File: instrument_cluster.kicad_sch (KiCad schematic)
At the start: 8 parts, among them J21 Conn_01x90_3Row_Socket

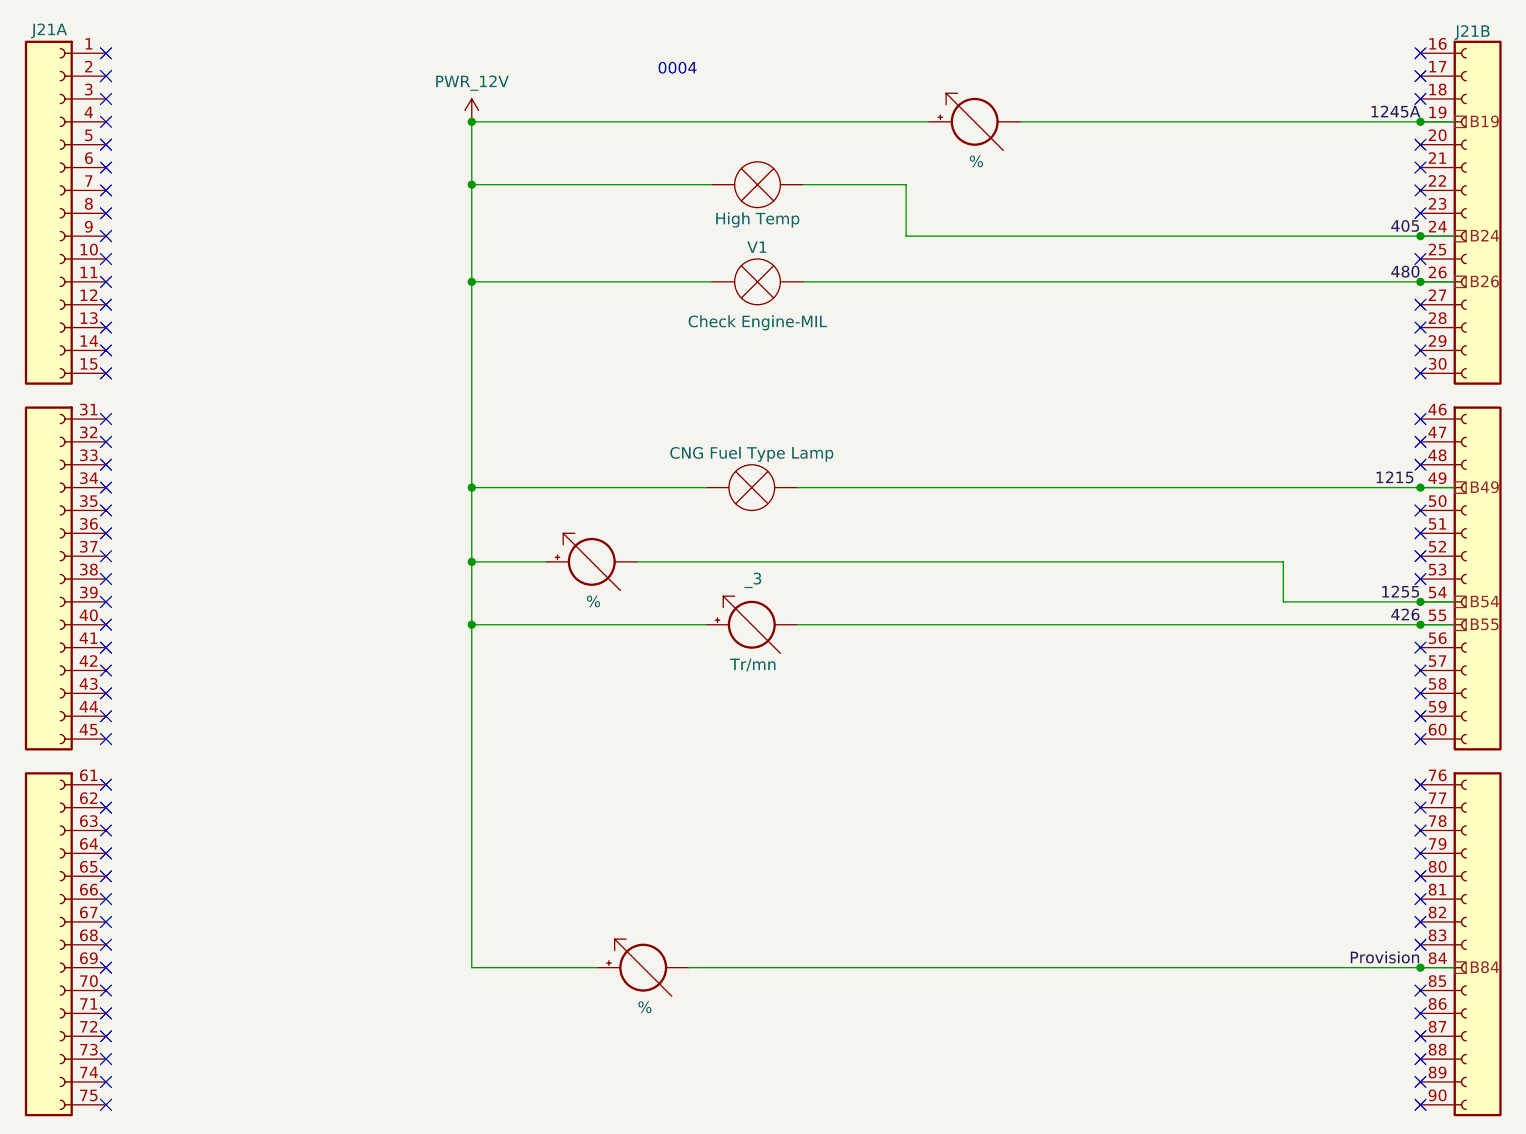
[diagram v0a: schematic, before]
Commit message: air conditioner updated
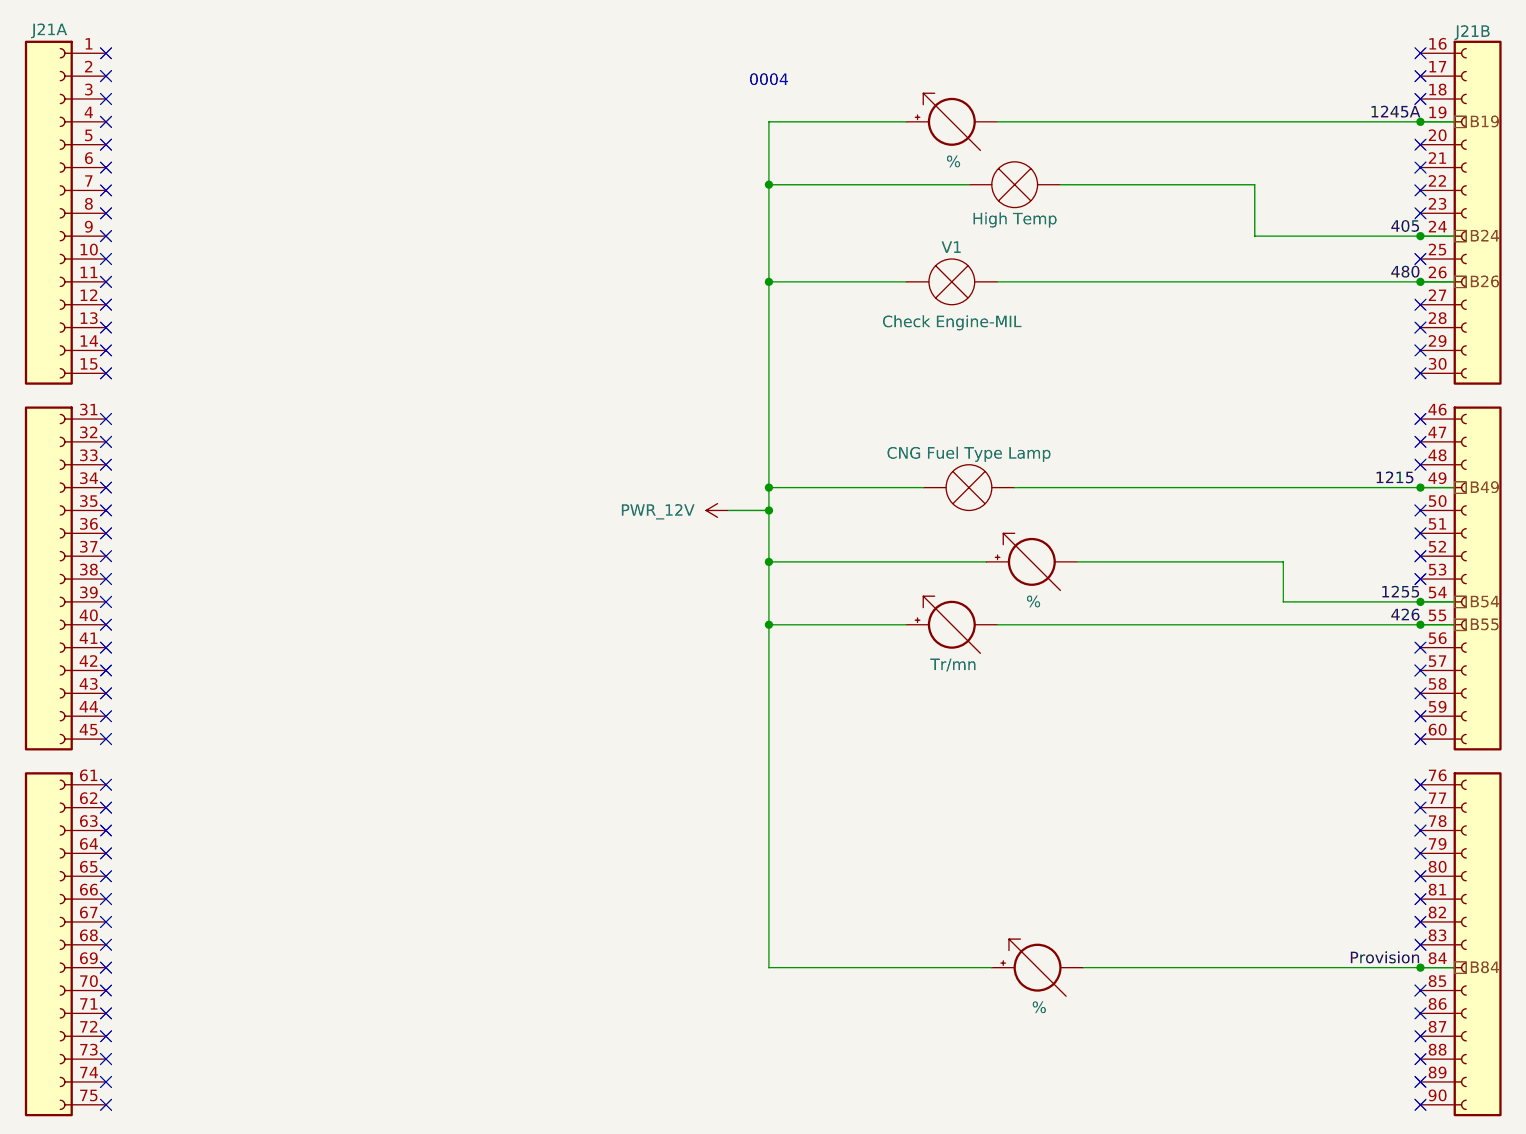
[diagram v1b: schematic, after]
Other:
- moved on the sheet: V1
